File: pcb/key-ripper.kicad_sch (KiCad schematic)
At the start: 186 parts, among them SW1 ESC, SW2 TILDE, SW3 TAB, SW4 CAPS, SW5 L_SHIFT, SW6 FN

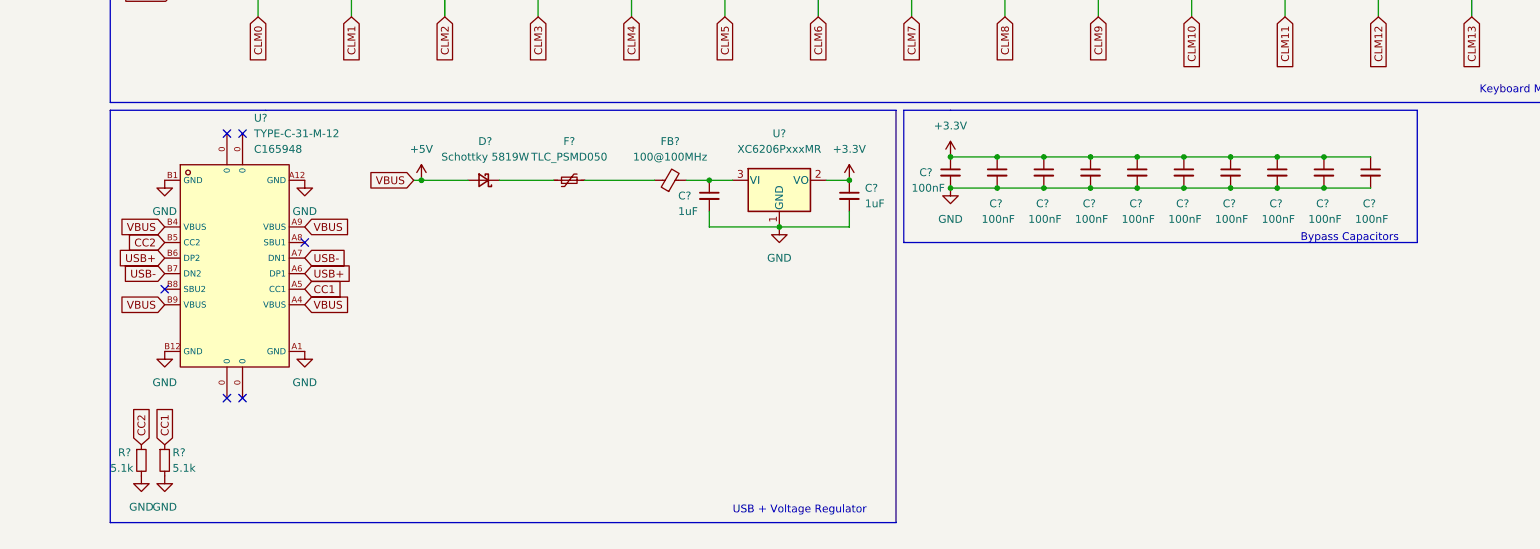
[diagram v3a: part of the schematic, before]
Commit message: Add power LED, tidy up schematic sections
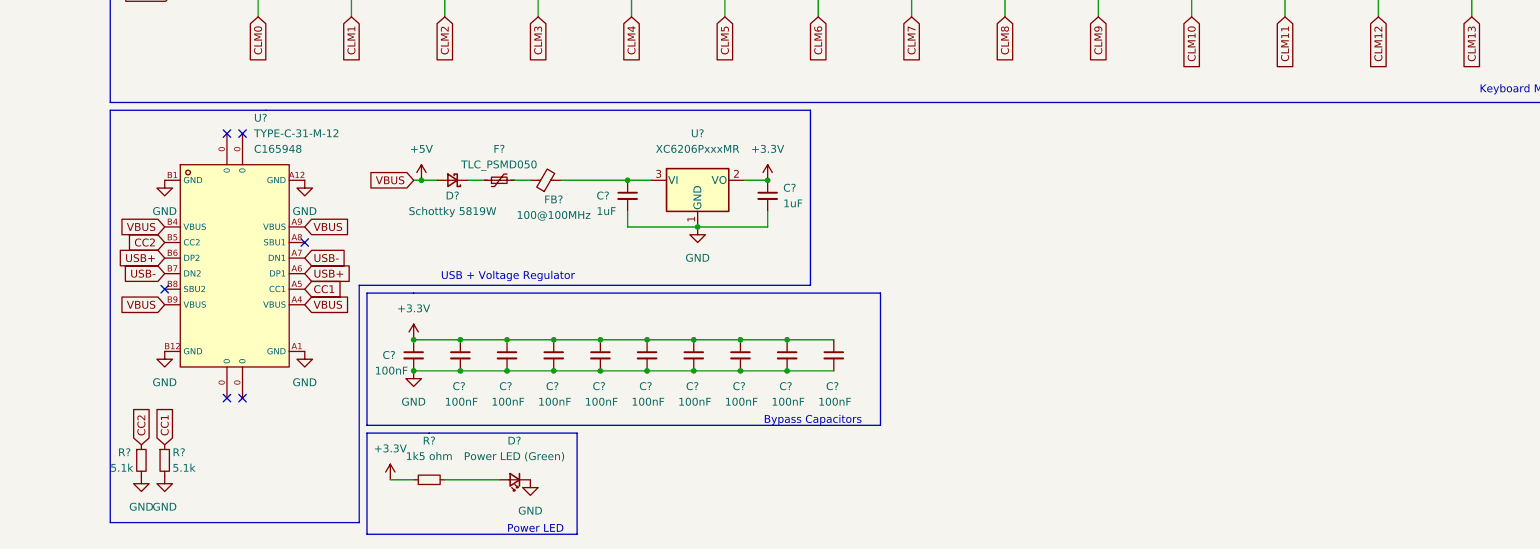
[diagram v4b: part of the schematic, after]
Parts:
- added D?: Power LED (Green), symbol Device:LED_Small
- added R?: 1k5 ohm, symbol Device:R_Small
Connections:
- net +3V3: now also R?.1
- net GND: now also D?.1 (K)
- new net: D?.2 (A), R?.2
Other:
- note added: "Power LED"
- moved on the sheet: C?, D?, F?, FB?, U?

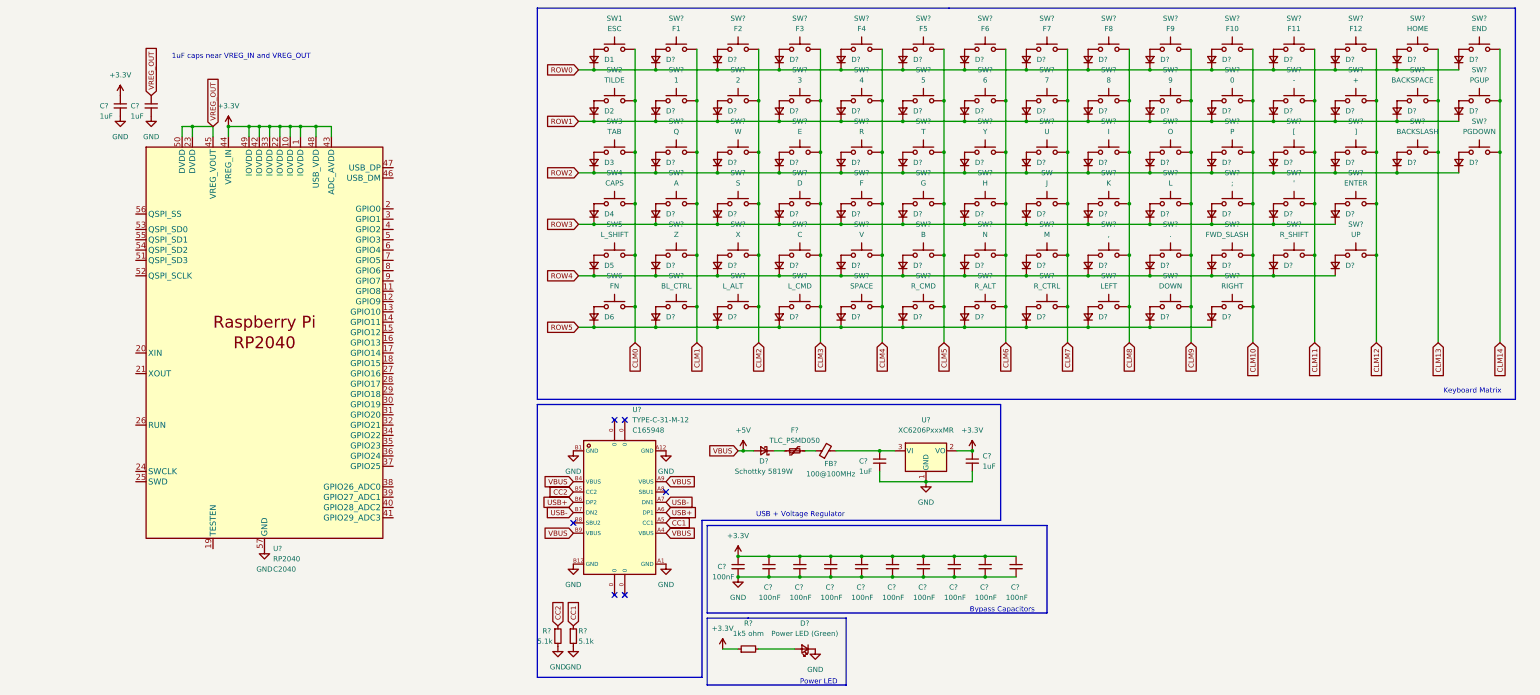
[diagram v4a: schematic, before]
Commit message: Add crystal oscillator, reset circuit, serial-wire debug circuits
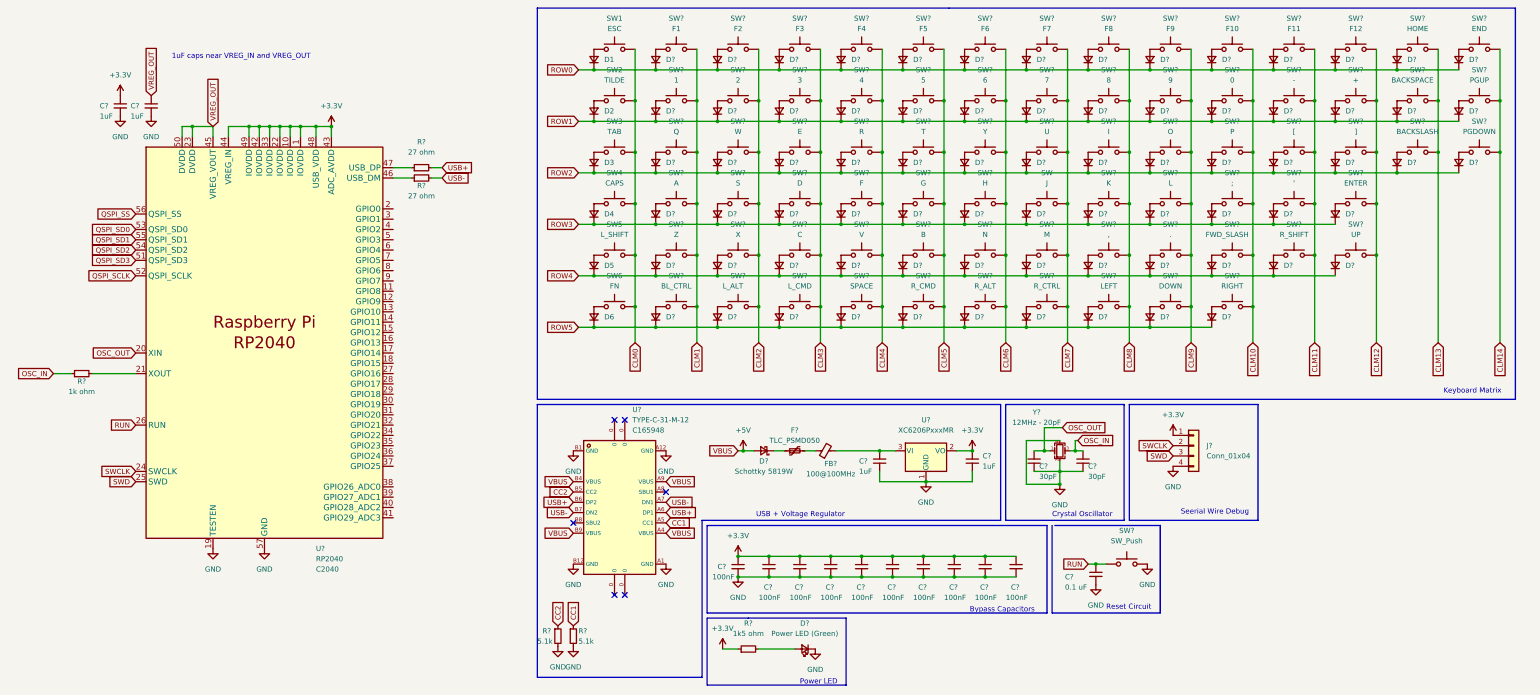
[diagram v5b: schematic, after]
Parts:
- added C?: 0.1 uF, symbol Device:C_Small
- added C? (x2): 30pF, symbol Device:C_Small
- added J?: Conn_01x04, symbol Connector_Generic:Conn_01x04
- added R? (x2): 27 ohm, symbol Device:R_Small
- added R?: 1k ohm, symbol Device:R_Small
- added SW?: SW_Push, symbol Switch:SW_Push
- added Y?: 12MHz - 20pF, symbol Device:Crystal_GND24_Small
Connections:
- net +3V3: now also J?.1 (Pin_1)
- net GND: now also U?.19 (TESTEN), C?.2, C?.2, C?.2, J?.4 (Pin_4), SW?.2, Y?.2, Y?.4
- net USB+: now also R?.2
- net USB-: now also R?.2
- net OSC_OUT: now reaches U?.20 (XIN)
- net OSC_OUT: now also C?.1, Y?.1
- net at U?.21 (XOUT): now also R?.2
- net SWCLK: now reaches U?.24 (SWCLK)
- net SWCLK: now also J?.2 (Pin_2)
- net SWD: now reaches U?.25 (SWD)
- net SWD: now also J?.3 (Pin_3)
- net RUN: now reaches U?.26 (RUN)
- net RUN: now also C?.1, SW?.1
- net at U?.46 (USB_DM): now also R?.1
- net at U?.47 (USB_DP): now also R?.1
- net QSPI_SD3: now reaches U?.51 (QSPI_SD3)
- net QSPI_SCLK: now reaches U?.52 (QSPI_SCLK)
- net QSPI_SD0: now reaches U?.53 (QSPI_SD0)
- net QSPI_SD2: now reaches U?.54 (QSPI_SD2)
- net QSPI_SD1: now reaches U?.55 (QSPI_SD1)
- net QSPI_SS: now reaches U?.56 (QSPI_SS)
- new net OSC_IN: C?.1, R?.1, Y?.3
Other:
- note added: "Crystal Oscillator"
- note added: "Reset Circuit"
- note added: "Seerial Wire Debug"

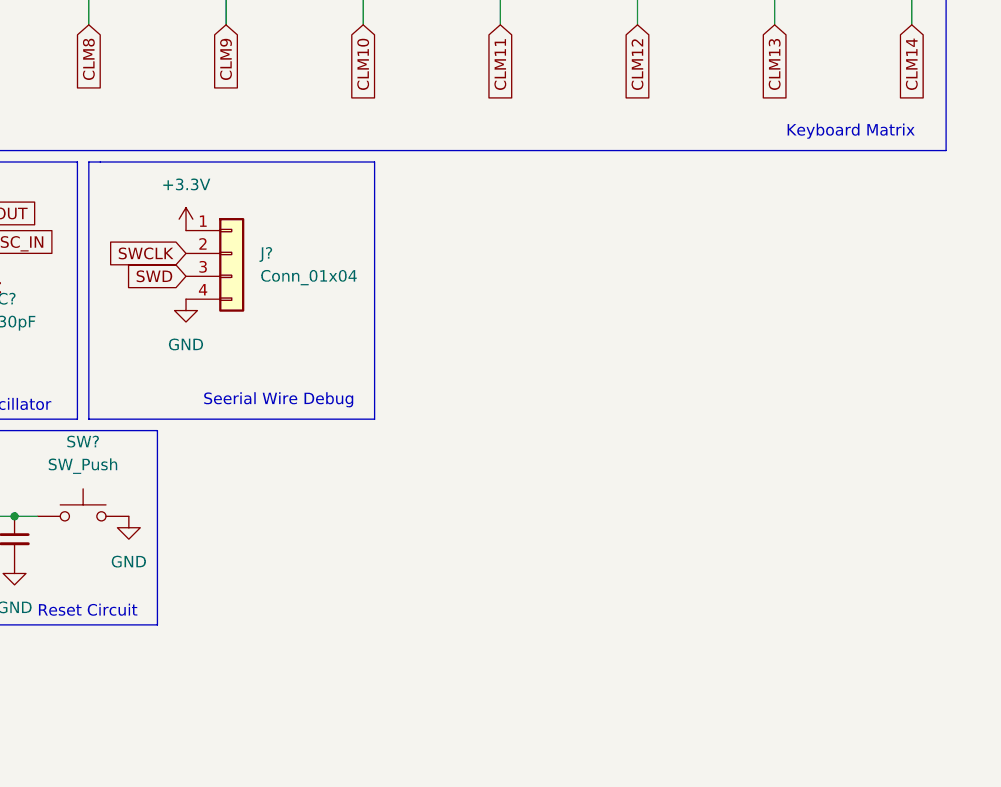
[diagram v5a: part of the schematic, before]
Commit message: Add the QSPI flash memory
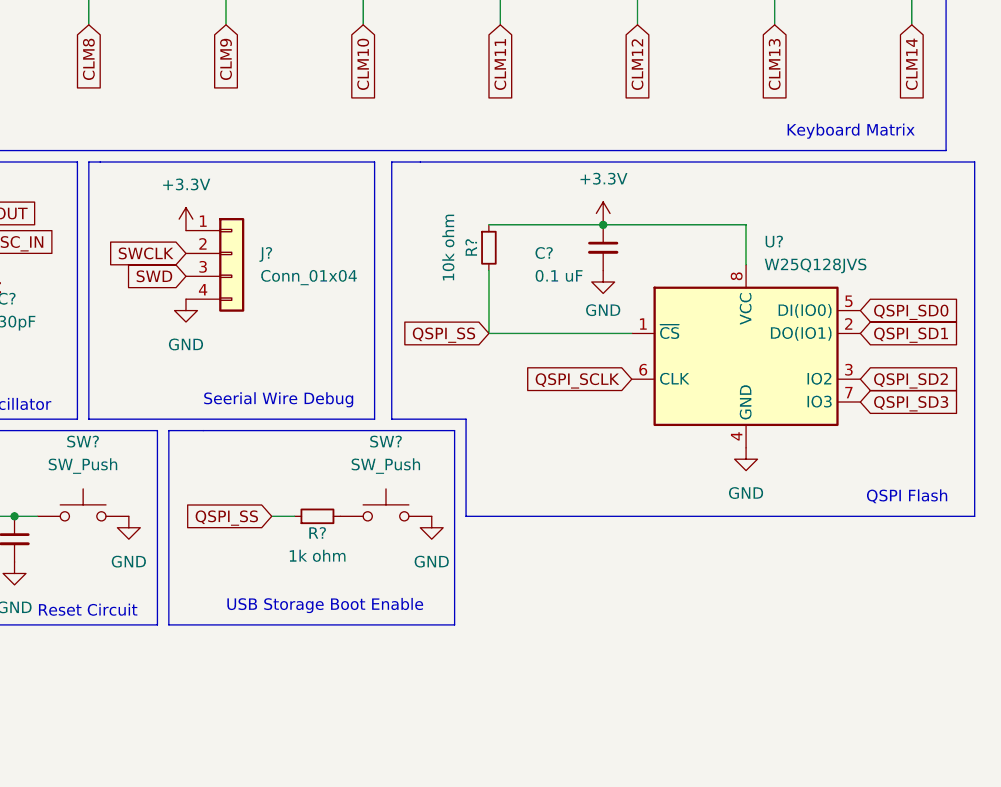
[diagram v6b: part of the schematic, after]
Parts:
- added C?: 0.1 uF, symbol Device:C_Small
- added R?: 10k ohm, symbol Device:R_Small
- added R?: 1k ohm, symbol Device:R_Small
- added SW?: SW_Push, symbol Switch:SW_Push
- added U?: W25Q128JVS, Package_SO:SOIC-8_5.23x5.23mm_P1.27mm, symbol Memory_Flash:W25Q128JVS
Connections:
- net +3V3: now also C?.1, R?.1, U?.8 (VCC)
- net GND: now also C?.2, SW?.2, U?.4 (GND)
- net QSPI_SCLK: now also U?.6 (CLK)
- net QSPI_SD0: now also U?.5 (DI(IO0))
- net QSPI_SD1: now also U?.2 (DO(IO1))
- net QSPI_SD2: now also U?.3 (IO2)
- net QSPI_SD3: now also U?.7 (IO3)
- net QSPI_SS: now also R?.1, R?.2, U?.1 (~{CS})
- new net: R?.2, SW?.1
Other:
- note added: "QSPI Flash"
- note added: "USB Storage Boot Enable"
